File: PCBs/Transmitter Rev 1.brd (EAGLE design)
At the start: 113 x 63.5 mm, 62 parts, among them J1 10118193-0001LF, T1 TEST_PAD, T10 TEST_PAD, T2 TEST_PAD, T3 TEST_PAD, T4 TEST_PAD, T5 TEST_PAD, T6 TEST_PAD, T7 TEST_PAD, T8 TEST_PAD, T9 TEST_PAD, U1 RFM95W-868S2, U2 TSRN_1-2450

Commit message: Route Board
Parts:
- moved T1 29.9 mm to (17.7, 21.1)
- moved CHG_C1 3.91 mm to (17.5, 39.4), turned to 0 degrees
- moved T10 3.70 mm to (10.5, 58.4)
- moved T4 3.47 mm to (21.0, 26.3)
- moved T5 3.18 mm to (16.0, 26.3)
- moved T7 3.14 mm to (21.3, 16.5)
- moved ALT_SWITCH 1.90 mm to (11.8, 24.8)
- moved CONV_C2 0.76 mm to (5.46, 29.3)
- moved T6 0.64 mm to (1.91, 23.5)
- moved CHIP_ANTENNA 0.63 mm to (109.9, 16.5)
- moved T8 0.63 mm to (96.0, 11.3)
- moved CONV_C3 0.38 mm to (4.83, 26.2)
- moved 9V_CON 0.25 mm to (95.0, 48.8), turned to 180 degrees
- moved CONV_C1 0.13 mm to (3.94, 40.1)
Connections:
- net SOURCE renamed DRAIN
- net UFL renamed N$1
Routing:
- net GND: track 30.3 -> 419.8 mm, vias 3 -> 19
- net VCC: track 0.00 -> 286.9 mm, vias 0 -> 4
- net VCC_5V: track 0.00 -> 221.2 mm, vias 0 -> 3
- net SPI1_MISO: track 0.00 -> 161.3 mm, vias 0 -> 3
- net I2C2_GPIO0/AIN_3.3V_0: track 0.00 -> 128.7 mm, vias 0 -> 2
- net UART2_GPIO1/PWM1: track 0.00 -> 127.7 mm, vias 0 -> 3
- net LI-PO_5V_OUT: track 24.0 -> 148.6 mm, vias 1 -> 4
- net RF_DIO1: track 0.00 -> 108.6 mm, vias 0 -> 1
- net I2C2_GPIO1/AIN_3.3V_1: track 0.00 -> 104.4 mm, vias 0 -> 3
- net SPI1_MOSI: track 0.00 -> 101.0 mm, vias 0 -> 7
- net UART1_GPIO0: track 0.00 -> 100.6 mm, vias 0 -> 2
- net N$26: track 0.00 -> 99.0 mm, vias 0 -> 1
- net N$29: track 0.00 -> 96.3 mm
- net RF_DIO4: track 0.00 -> 95.7 mm, vias 0 -> 3
- net N$21: track 0.00 -> 95.6 mm, vias 0 -> 2
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
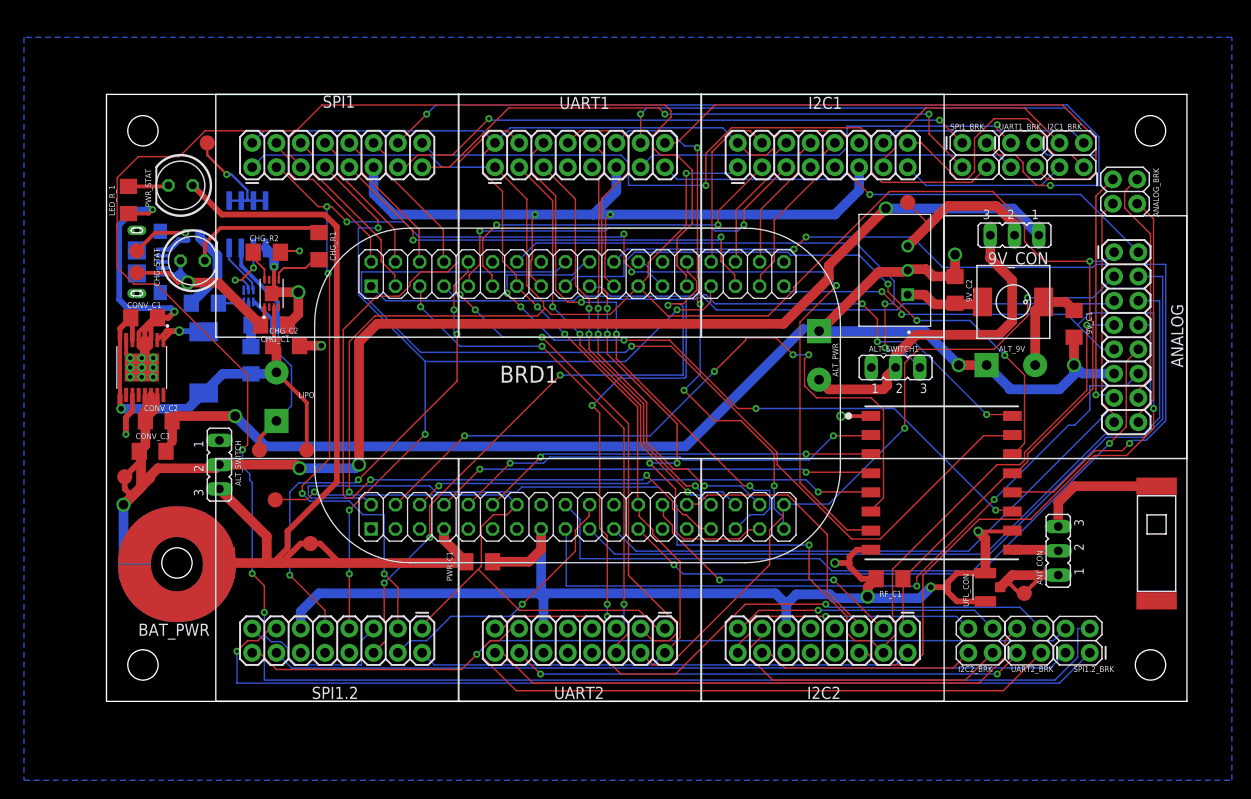
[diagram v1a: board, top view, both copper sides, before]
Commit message: Increase size of and reroute VCC and VCC_5V traces throughout the board
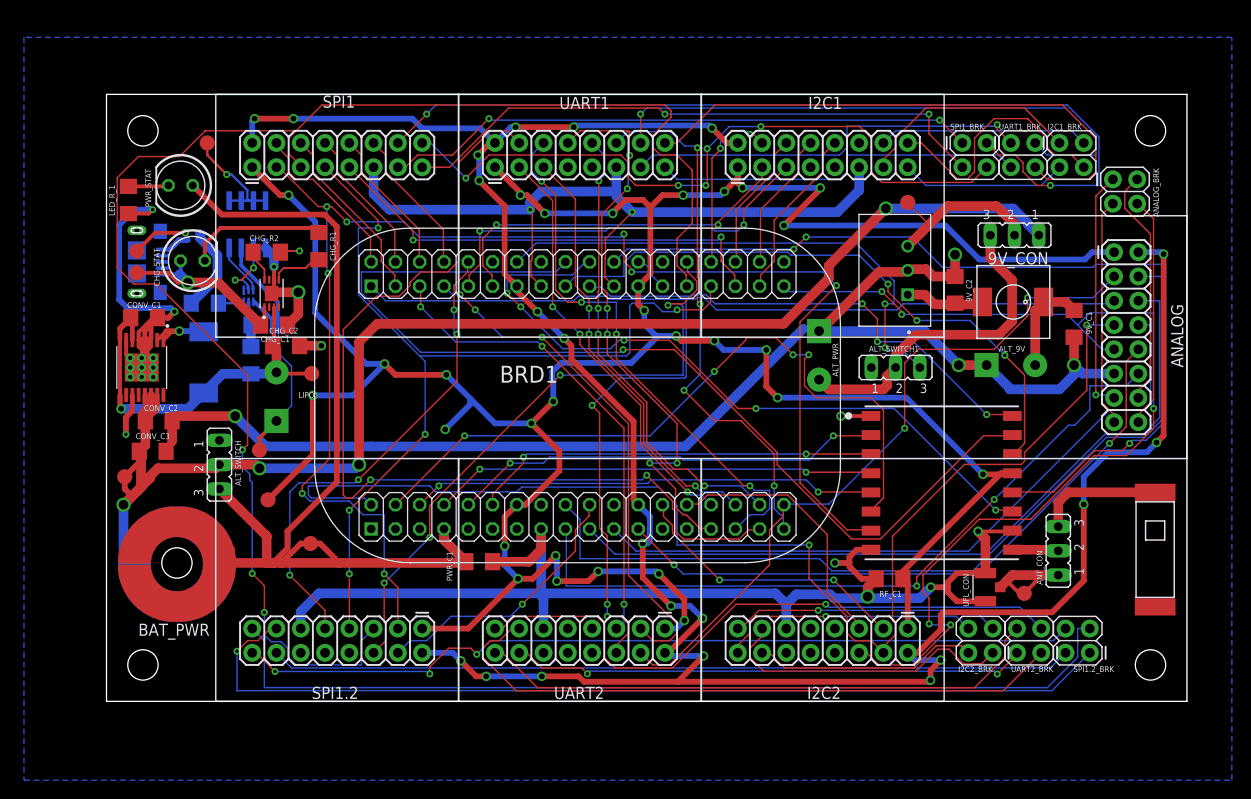
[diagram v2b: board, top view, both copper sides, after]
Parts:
- moved T4 8.02 mm to (21.5, 34.3)
- moved T1 0.76 mm to (16.9, 21.1)
- moved CHIP_ANTENNA 0.65 mm to (109.7, 15.9)
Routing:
- net VCC_5V: track 221.2 -> 257.8 mm, vias 3 -> 21
- net VCC: track 286.9 -> 315.6 mm, vias 4 -> 28
- net LI-PO_+: track 46.8 -> 41.1 mm
- net SPI1_CLK: track 92.9 -> 96.9 mm
- net I2C2_GPIO1/AIN_3.3V_1: track 104.4 -> 108.1 mm, vias 3 -> 5
- net I2C2_GPIO0/AIN_3.3V_0: track 128.7 -> 130.8 mm
- net GND: track 419.8 -> 417.8 mm
- net N$25: track 71.8 -> 73.7 mm, vias 1 -> 5
- net N$28: track 87.6 -> 88.9 mm, vias 1 -> 3
- net N$29: track 96.3 -> 97.4 mm
- net N$26: track 99.0 -> 100.1 mm
- net RF_MOSI: track 41.8 -> 42.8 mm
- net RF_DIO3: track 73.5 -> 74.3 mm
- net N$45: track 22.9 -> 23.5 mm
- net UART1_GPIO2: track 58.8 -> 59.4 mm, vias 4 -> 6
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
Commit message: Update EAGLE version and small miscellaneous documentation/functionality fixes
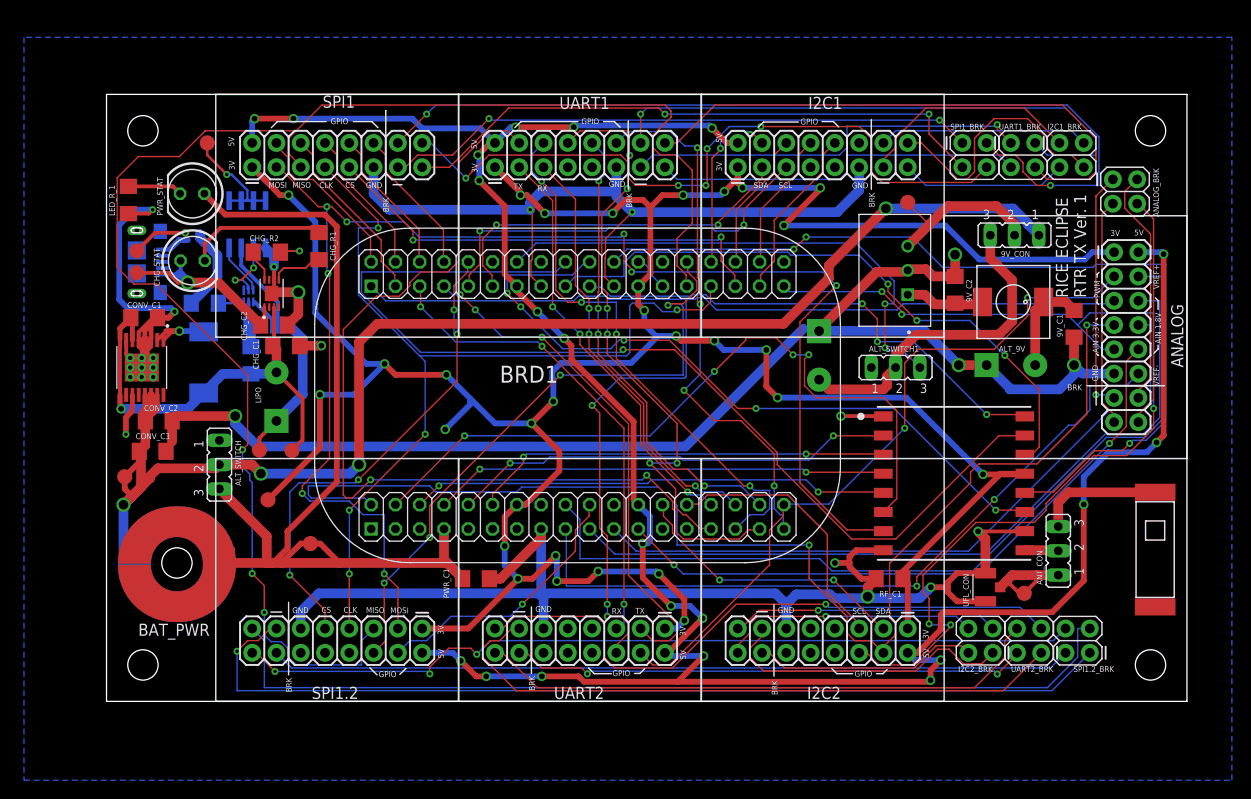
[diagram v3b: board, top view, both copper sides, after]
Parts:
- moved T4 8.31 mm to (19.4, 26.2)
- moved PWR_C1 1.81 mm to (38.7, 12.8)
- moved PWR_STAT 1.49 mm to (8.97, 53.1)
- moved U1 1.30 mm to (88.7, 22.8)
- flipped ALT_PWR to the bottom
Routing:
- net LI-PO_+: track 41.1 -> 47.1 mm
- net GND: track 417.8 -> 422.7 mm
- net VCC: track 315.6 -> 317.8 mm
- net LI-PO_-: track 28.3 -> 29.9 mm
- net LED: track 4.23 -> 5.73 mm
- net RF_RST: track 75.2 -> 76.7 mm
- net RF_DIO2: track 51.5 -> 52.8 mm
- net RF_DIO3: track 74.3 -> 75.6 mm
- net RF_ANT: track 4.84 -> 3.52 mm
- net RF_CLK: track 46.4 -> 47.7 mm
- net RF_DIO5: track 53.5 -> 54.8 mm
- net RF_CS: track 48.8 -> 50.1 mm
- net RF_MOSI: track 42.8 -> 44.1 mm
- net RF_DIO4: track 95.7 -> 94.4 mm
- net RF_MISO: track 45.4 -> 46.7 mm
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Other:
- board text added: "+"
- board text added: "3V"
- board text added: "5V"
- board text added: "9V_PWR"
- board text added: "AIN 1.8V"
- board text added: "AIN 3.3V"
- board text added: "BRK"
- board text added: "CLK"
- board text added: "CS"
- board text added: "GND"
- board text added: "GPIO"
- board text added: "MISO"
- board text added: "MOSI"
- board text added: "PWM"
- board text added: "RICE ECLIPSE RTR TX Ver. 1"
- board text added: "RX"
- board text added: "SCL"
- board text added: "SDA"
- board text added: "TX"
- board text added: "VREF+"
- board text added: "VREF-"
- board text added: "_"
